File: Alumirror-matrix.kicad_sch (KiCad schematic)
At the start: 54 parts, among them K00 PG1350, K01 PG1350, K02 PG1350, K03 PG1350, K04 PG1350, K05 PG1350, K10 PG1350, K11 PG1350, K12 PG1350, K13 PG1350, K14 PG1350, K15 PG1350, K20 PG1350, K21 PG1350, K22 PG1350, K23 PG1350, K24 PG1350, K25 PG1350_1½U, K30 PG1350_1½U, K31 PG1350/SKQUCAA010

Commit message: Renumber components
 * For single-digit components:
   * Odd numbers are populated on the lefthand board only
   * Even numbers are populated on the righthand board only
 * Double-digit components are populated on both sides
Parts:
- renumbered R1 to R11, R2 to R12, R3 to R13, R4 to R14, R5 to R15, R6 to R16, R7 to R17, R8 to R18, R9 to R19, R10 to R20
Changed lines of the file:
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@@
 		(dnp no)
 		(fields_autoplaced yes)
-		(property "Reference" "R3"
+		(property "Reference" "R13"
 			(at 146.05 44.4499 0)
 			(effects
@@
 			(project "Alumirror"
 				(path "/52f043ac-ccff-4c85-bc10-2db9d3c9e3f3/ba0213d9-9934-4194-9bec-bf394cd27126"
-					(reference "R3")
+					(reference "R13")
 					(unit 1)
 				)
@@
 		(on_board yes)
 		(dnp no)
-		(property "Reference" "R1"
+		(property "Reference" "R11"
 			(at 90.17 59.6899 0)
 			(effects
@@
 			(project "Alumirror"
 				(path "/52f043ac-ccff-4c85-bc10-2db9d3c9e3f3/ba0213d9-9934-4194-9bec-bf394cd27126"
-					(reference "R1")
+					(reference "R11")
 					(unit 1)
 				)
@@
 		(dnp no)
 		(fields_autoplaced yes)
-		(property "Reference" "R9"
+		(property "Reference" "R19"
 			(at 173.99 72.3899 0)
 			(effects
@@
 			(project "Alumirror"
 				(path "/52f043ac-ccff-4c85-bc10-2db9d3c9e3f3/ba0213d9-9934-4194-9bec-bf394cd27126"
-					(reference "R9")
+					(reference "R19")
 					(unit 1)
 				)
@@
 		(dnp no)
 		(fields_autoplaced yes)
-		(property "Reference" "R6"
+		(property "Reference" "R16"
 			(at 229.87 59.6899 0)
 			(effects
@@
 			(project "Alumirror"
 				(path "/52f043ac-ccff-4c85-bc10-2db9d3c9e3f3/ba0213d9-9934-4194-9bec-bf394cd27126"
-					(reference "R6")
+					(reference "R16")
 					(unit 1)
 				)
@@
 		(on_board yes)
 		(dnp no)
-		(property "Reference" "R2"
+		(property "Reference" "R12"
 			(at 118.11 49.5299 0)
 			(effects
@@
 			(project "Alumirror"
 				(path "/52f043ac-ccff-4c85-bc10-2db9d3c9e3f3/ba0213d9-9934-4194-9bec-bf394cd27126"
-					(reference "R2")
+					(reference "R12")
 					(unit 1)
 				)
@@
 		(dnp no)
 		(fields_autoplaced yes)
-		(property "Reference" "R4"
+		(property "Reference" "R14"
 			(at 173.99 44.4499 0)
 			(effects
@@
 			(project "Alumirror"
 				(path "/52f043ac-ccff-4c85-bc10-2db9d3c9e3f3/ba0213d9-9934-4194-9bec-bf394cd27126"
-					(reference "R4")
+					(reference "R14")
 					(unit 1)
 				)
@@
 		(dnp no)
 		(fields_autoplaced yes)
-		(property "Reference" "R8"
+		(property "Reference" "R18"
 			(at 146.05 72.3899 0)
 			(effects
@@
 			(project "Alumirror"
 				(path "/52f043ac-ccff-4c85-bc10-2db9d3c9e3f3/ba0213d9-9934-4194-9bec-bf394cd27126"
-					(reference "R8")
+					(reference "R18")
 					(unit 1)
 				)
@@
 		(dnp no)
 		(fields_autoplaced yes)
-		(property "Reference" "R7"
+		(property "Reference" "R17"
 			(at 118.11 77.4699 0)
 			(effects
@@
 			(project "Alumirror"
 				(path "/52f043ac-ccff-4c85-bc10-2db9d3c9e3f3/ba0213d9-9934-4194-9bec-bf394cd27126"
-					(reference "R7")
+					(reference "R17")
 					(unit 1)
 				)
@@
 		(on_board yes)
 		(dnp no)
-		(property "Reference" "R10"
+		(property "Reference" "R20"
 			(at 201.93 77.4699 0)
 			(effects
@@
 			(project "Alumirror"
 				(path "/52f043ac-ccff-4c85-bc10-2db9d3c9e3f3/ba0213d9-9934-4194-9bec-bf394cd27126"
-					(reference "R10")
+					(reference "R20")
 					(unit 1)
 				)
@@
 		(dnp no)
 		(fields_autoplaced yes)
-		(property "Reference" "R5"
+		(property "Reference" "R15"
 			(at 201.93 49.5299 0)
 			(effects
@@
 			(project "Alumirror"
 				(path "/52f043ac-ccff-4c85-bc10-2db9d3c9e3f3/ba0213d9-9934-4194-9bec-bf394cd27126"
-					(reference "R5")
+					(reference "R15")
 					(unit 1)
 				)

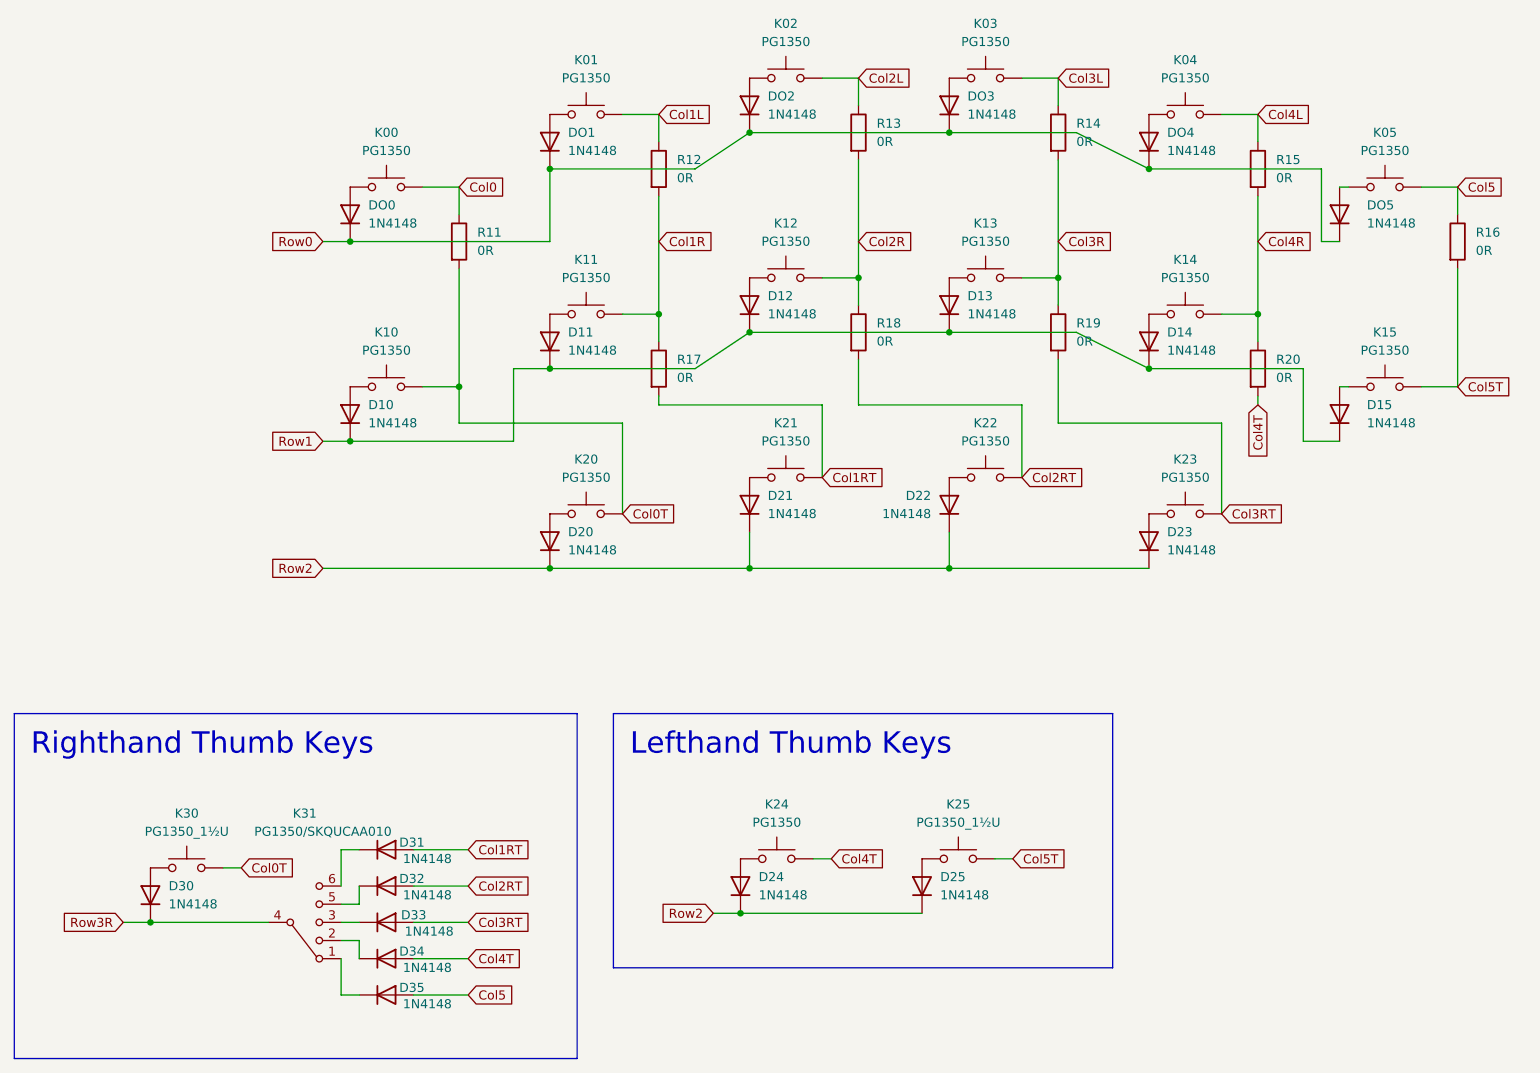
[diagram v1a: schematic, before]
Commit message: Renumber matrix switches and diodes
Columns and rows start from 1 rather than 0.
All components now follow the rules from the previous change, and we don’t had to mess around with the fake D-“oh” nonsense.
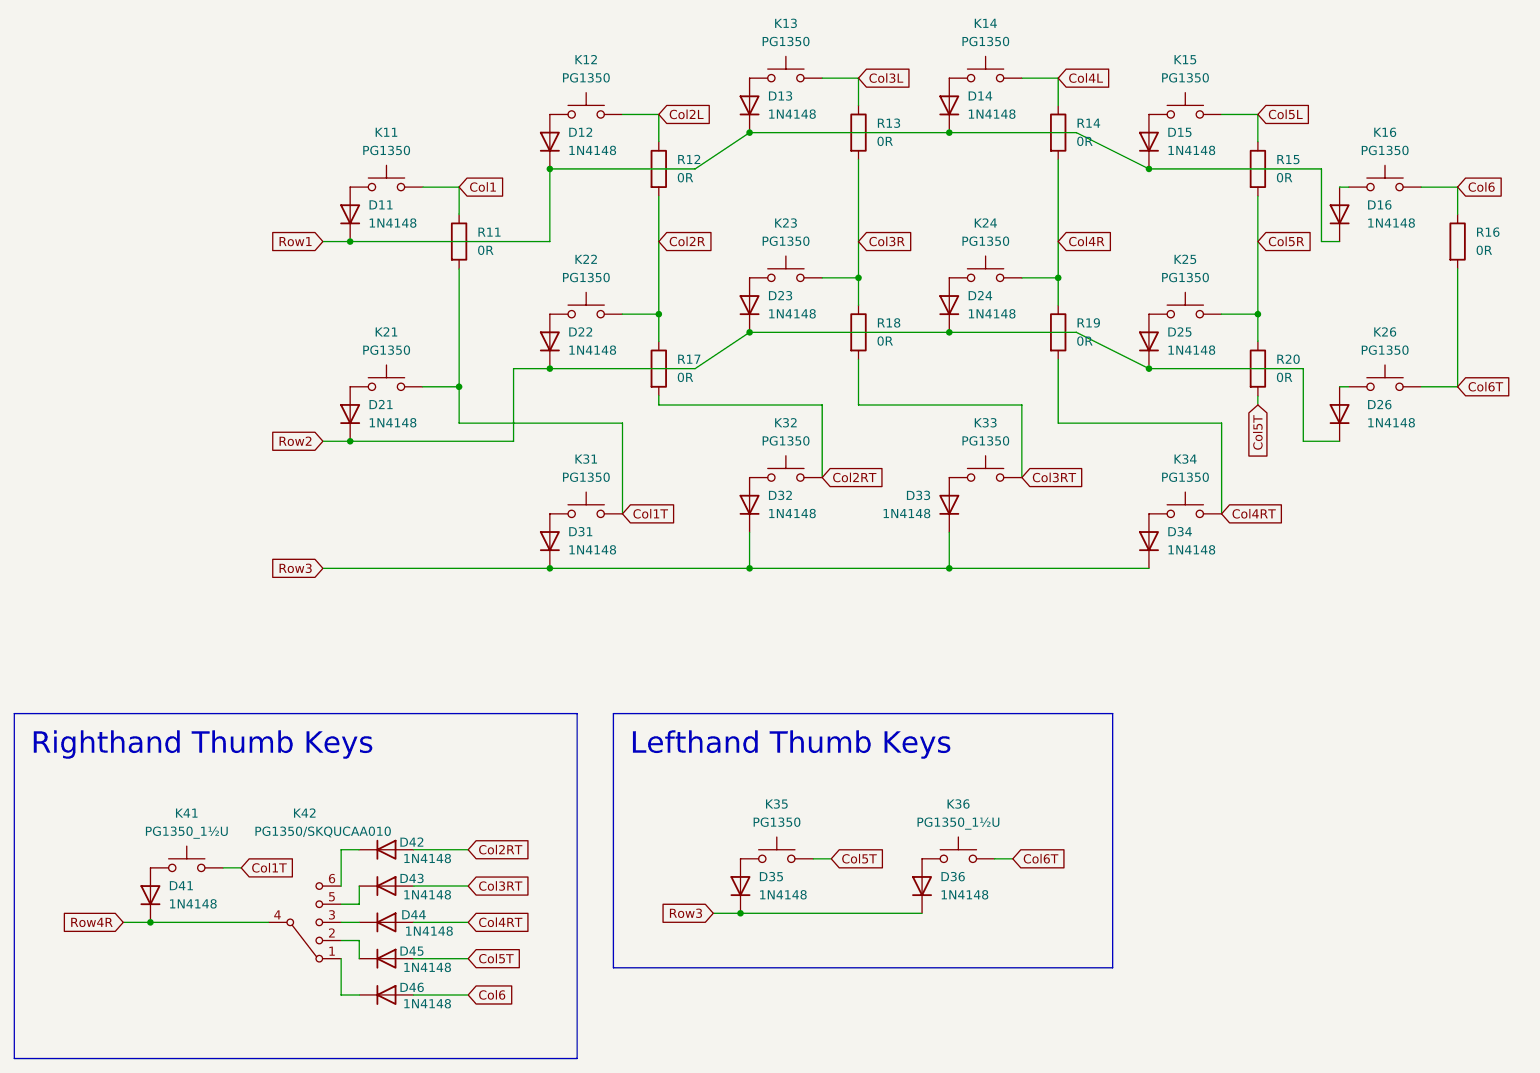
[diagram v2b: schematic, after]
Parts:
- renumbered DO0 to D11, DO1 to D12, DO2 to D13, DO3 to D14, DO4 to D15, DO5 to D16, D10 to D21, D11 to D22, D12 to D23, D13 to D24, D14 to D25, D15 to D26, D20 to D31, D21 to D32, D22 to D33, D23 to D34, D24 to D35, D25 to D36, D30 to D41, D31 to D42, D32 to D43, D33 to D44, D34 to D45, D35 to D46, K00 to K11, K01 to K12, K02 to K13, K03 to K14, K04 to K15, K05 to K16, K10 to K21, K11 to K22, K12 to K23, K13 to K24, K14 to K25, K15 to K26, K20 to K31, K21 to K32, K22 to K33, K23 to K34, K24 to K35, K25 to K36, K30 to K41, K31 to K42
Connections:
- net Col1L is gone; now on net Col2L: K12.1, R12.1
- net Col1R is gone; now on net Col2R: K22.1, R12.2, R17.1
- net Col1RT is gone; now on net Col2RT: D42.2 (A), K32.1, R17.2
- net Col4T is gone; now on net Col5T: D45.2 (A), K35.1, R20.2
- net Row0 is gone; now on net Row1: D11.1 (K), D12.1 (K), D13.1 (K), D14.1 (K), D15.1 (K), D16.1 (K)
- net Col2L: no longer K13.1, R13.1
- net Col2R: no longer K23.1, R13.2, R18.1
- net Col2RT: no longer D43.2 (A), K33.1, R18.2
- net Col3L: now also K13.1, R13.1; no longer K14.1, R14.1
- net Col3R: now also K23.1, R13.2, R18.1; no longer K24.1, R14.2, R19.1
- net Col3RT: now also D43.2 (A), K33.1, R18.2; no longer D44.2 (A), K34.1, R19.2
- net Col4L: now also K14.1, R14.1; no longer K15.1, R15.1
- net Col4R: now also K24.1, R14.2, R19.1; no longer K25.1, R15.2, R20.1
- net Col5T: no longer K26.1, K36.1, R16.2
- net Row1: no longer D21.1 (K), D22.1 (K), D23.1 (K), D24.1 (K), D25.1 (K), D26.1 (K)
- net Row2: now also D21.1 (K), D22.1 (K), D23.1 (K), D24.1 (K), D25.1 (K), D26.1 (K); no longer D31.1 (K), D32.1 (K), D33.1 (K), D34.1 (K), D35.1 (K), D36.1 (K)
- net Col0 renamed Col1
- net Col0T renamed Col1T
- net Col5 renamed Col6
- net Row3R renamed Row4R
- new net Col4RT: D44.2 (A), K34.1, R19.2
- new net Col5L: K15.1, R15.1
- new net Col5R: K25.1, R15.2, R20.1
- new net Col6T: K26.1, K36.1, R16.2
- new net Row3: D31.1 (K), D32.1 (K), D33.1 (K), D34.1 (K), D35.1 (K), D36.1 (K)

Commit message: Switch K22 to new “clipped” footprint
Clipped footprint has a cut-out in one of the hot-swap socket pads to avoid proximity warning with solder nut pad.
Also tweaked and rounded multiple traces.
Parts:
- K22: footprint Project Library:SW_choc_v1_HS_CPG135001S30_1layer_1u -> Project Library:SW_choc_v1_HS_CPG135001S30_1layer_1u_clipped
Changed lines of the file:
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@@
 			)
 		)
-		(property "Footprint" "Project Library:SW_choc_v1_HS_CPG135001S30_1layer_1u"
+		(property "Footprint" "Project Library:SW_choc_v1_HS_CPG135001S30_1layer_1u_clipped"
 			(at 105.41 66.04 0)
 			(effects

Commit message: Remove need for clipped hot-swap footprint
Moved mounting holes up 1/48U allowing K22 to be a regular socket. The mounting hole should still not interfere with the surrounding switches.
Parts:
- K22: footprint Project Library:SW_choc_v1_HS_CPG135001S30_1layer_1u_clipped -> Project Library:SW_choc_v1_HS_CPG135001S30_1layer_1u
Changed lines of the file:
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@@
 			)
 		)
-		(property "Footprint" "Project Library:SW_choc_v1_HS_CPG135001S30_1layer_1u_clipped"
+		(property "Footprint" "Project Library:SW_choc_v1_HS_CPG135001S30_1layer_1u"
 			(at 105.41 66.04 0)
 			(effects
